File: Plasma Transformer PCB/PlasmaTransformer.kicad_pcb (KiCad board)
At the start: 2 copper layers, 90 x 90 mm, 65 parts, among them J1 Barrel_Jack_MountingPin, J11 Screw_Terminal_01x01, J12 Screw_Terminal_01x01, J2 Conn_01x02_Pin, J3 Conn_Coaxial, J4 Conn_02x04_Odd_Even, J5 Conn_Coaxial, J6 Conn_02x04_Odd_Even, J8 AudioJack3, M1 Fan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

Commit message: convert tank caps to push fit sockets
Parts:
- added J10: Conn_01x01_Socket, ALibrary:H8501-05, F.Cu at (89.0, 121.5)
- added J13: Conn_01x01_Socket, ALibrary:H8501-05, F.Cu at (89.0, 111.5)
- added J14: Conn_01x01_Socket, ALibrary:H8501-05, F.Cu at (83.5, 121.5)
- added J15: Conn_01x01_Socket, ALibrary:H8501-05, F.Cu at (83.5, 111.5)
- added J16: Conn_01x01_Socket, ALibrary:H8501-05, F.Cu at (78.0, 121.5)
- added J17: Conn_01x01_Socket, ALibrary:H8501-05, F.Cu at (78.0, 111.5)
- added J18: Conn_01x01_Socket, ALibrary:H8501-05, F.Cu at (72.5, 121.5)
- added J19: Conn_01x01_Socket, ALibrary:H8501-05, F.Cu at (72.5, 111.5)
- added J20: Conn_01x01_Socket, ALibrary:H8501-05, F.Cu at (67.0, 121.5)
- added J21: Conn_01x01_Socket, ALibrary:H8501-05, F.Cu at (67.0, 111.5)
- added J7: Conn_01x01_Socket, ALibrary:H8501-05, F.Cu at (94.5, 121.5)
- added J9: Conn_01x01_Socket, ALibrary:H8501-05, F.Cu at (94.5, 111.5)

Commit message: WIP rev 5 rebase
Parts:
- removed J10, J13, J14, J15, J16, J17, J18, J19, J20, J21, J7, J9: Conn_01x01_Socket, ALibrary:H8501-05
- added C25: 4.7uF, Capacitor_SMD:C_1210_3225Metric, F.Cu at (155.3, 96.6)
- added C26: 4.7uF, Capacitor_SMD:C_1210_3225Metric, F.Cu at (155.3, 100.8)
- added C27: 100nF, Capacitor_SMD:C_0805_2012Metric, F.Cu at (169.1, 82.4)
- added C28: 100nF, Capacitor_SMD:C_0805_2012Metric, F.Cu at (169.1, 85.4)
- added C29: 22uF, Capacitor_SMD:C_0805_2012Metric, F.Cu at (169.1, 88.4)
- added L3: 56uH, Inductor_SMD:L_Bourns_SRR1210A, F.Cu at (159.7, 87.7)
- added R1: 100k, Resistor_SMD:R_0805_2012Metric, F.Cu at (160.3, 95.9)
- added R10: 7.15k, Resistor_SMD:R_0805_2012Metric, F.Cu at (160.3, 98.9)
- added U1: LMR51610YDBVR, Package_TO_SOT_SMD:SOT-23-6, F.Cu at (165.1, 96.8)
- D5, D6, D7, D8: footprint Diode_SMD:D_SMB -> Diode_SMD:D_SMF
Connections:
- net Net-(D1-K) renamed /REF10V
- net Net-(SW1-A) renamed /VIN
- C1 pad 1: Net-(J10-Pin_1) -> Net-(J12-Pin_1)
- C12 pad 2: Net-(J2-Pin_1) -> +V
- C13 pad 2: Net-(J2-Pin_1) -> +V
- C14 pad 1: Net-(J10-Pin_1) -> /DRAIN
- C16 pad 1: Net-(J10-Pin_1) -> Net-(J12-Pin_1)
- C17 pad 1: Net-(J10-Pin_1) -> Net-(J12-Pin_1)
- C18 pad 1: Net-(J10-Pin_1) -> Net-(J12-Pin_1)
- C19 pad 1: Net-(J10-Pin_1) -> Net-(J12-Pin_1)
- C2 pad 1: Net-(J2-Pin_1) -> +V
- C20 pad 1: Net-(J10-Pin_1) -> Net-(J12-Pin_1)
- J12 pad 1: Net-(J10-Pin_1) -> Net-(J12-Pin_1)
- J2 pad 1: Net-(J2-Pin_1) -> +12V
- L2 pad 1: Net-(J2-Pin_1) -> +V
- R2 pad 1: Net-(J2-Pin_1) -> +12V
- SW1 pad 2: Net-(J2-Pin_1) -> +V
- TP2 pad 1: Net-(J2-Pin_1) -> +V
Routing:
- net Net-(J2-Pin_1): track 128.0 -> 0.00 mm
- net (no net): track 0.00 -> 128.0 mm
- net Net-(J12-Pin_1): track 0.00 -> 78.5 mm
- net Net-(J10-Pin_1): track 78.5 -> 0.00 mm
- net Net-(D6-A): track 70.2 -> 71.8 mm
- net Net-(D5-K): track 51.4 -> 50.7 mm
- added copper zone on F.Cu, net +V
- removed copper zone on F.Cu, net Net-(J2-Pin_1)
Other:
- board text added: "REV 5 SEPT 2025 E. CHIU"
- board text removed: "REV 4 JULY 2025 E. CHIU"

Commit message: WIP layout
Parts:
- L3: value 56uH -> 22uH; footprint Inductor_SMD:L_Bourns_SRR1210A -> Inductor_SMD:L_Coilcraft_2222SQ-90N
- moved C28 35.6 mm to (133.6, 88.0), turned to 90 degrees
- moved C27 34.3 mm to (134.8, 81.4), turned to 180 degrees
- moved U1 32.4 mm to (135.2, 84.2), turned to 180 degrees
- moved C26 29.9 mm to (135.3, 78.5)
- moved C25 29.4 mm to (135.3, 75.0)
- moved C29 25.4 mm to (143.7, 88.1), turned to 90 degrees
- moved R10 25.0 mm to (139.4, 85.1), turned to 180 degrees
- moved L3 20.9 mm to (138.9, 89.8)
- moved R1 20.4 mm to (143.0, 85.1), turned to 180 degrees
- moved TP2 2.32 mm to (140.2, 95.3)
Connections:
- net Net-(U1-SW) renamed /12VSW
- C14 pad 1: /DRAIN -> Net-(J12-Pin_1)
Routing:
- net (no net): track 128.0 -> 0.00 mm
- net +V: track 0.00 -> 123.5 mm, vias 0 -> 1
- net +12V: track 0.00 -> 103.8 mm, vias 0 -> 2
- net GND: track 354.3 -> 369.4 mm, vias 8 -> 11
- net Net-(U1-FB): track 0.00 -> 8.34 mm
- net Net-(U1-CB): track 0.00 -> 3.12 mm
- added copper zone on F.Cu, net /12VSW
- added copper zone on B.Cu, net GND
- added copper zone on F.Cu, net GND

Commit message: WIP layout
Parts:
- moved J3 1.50 mm to (61.0, 92.0)
- moved J5 1.50 mm to (61.0, 78.0)
- moved R8 1.00 mm to (69.0, 78.1)
- moved R7 1.00 mm to (67.2, 85.2)
- moved C25 0.40 mm to (135.7, 75.0)
- moved C26 0.40 mm to (135.7, 78.5)
- moved C27 0.40 mm to (135.2, 81.4)
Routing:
- net /DRAIN: track 175.2 -> 173.4 mm
- net Net-(J3-In): track 10.6 -> 11.9 mm
- net +V: track 123.5 -> 122.3 mm
- net /GATE: track 82.2 -> 81.1 mm
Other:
- board text added: "12- 60V IN"
- board text removed: "15- 24V IN"

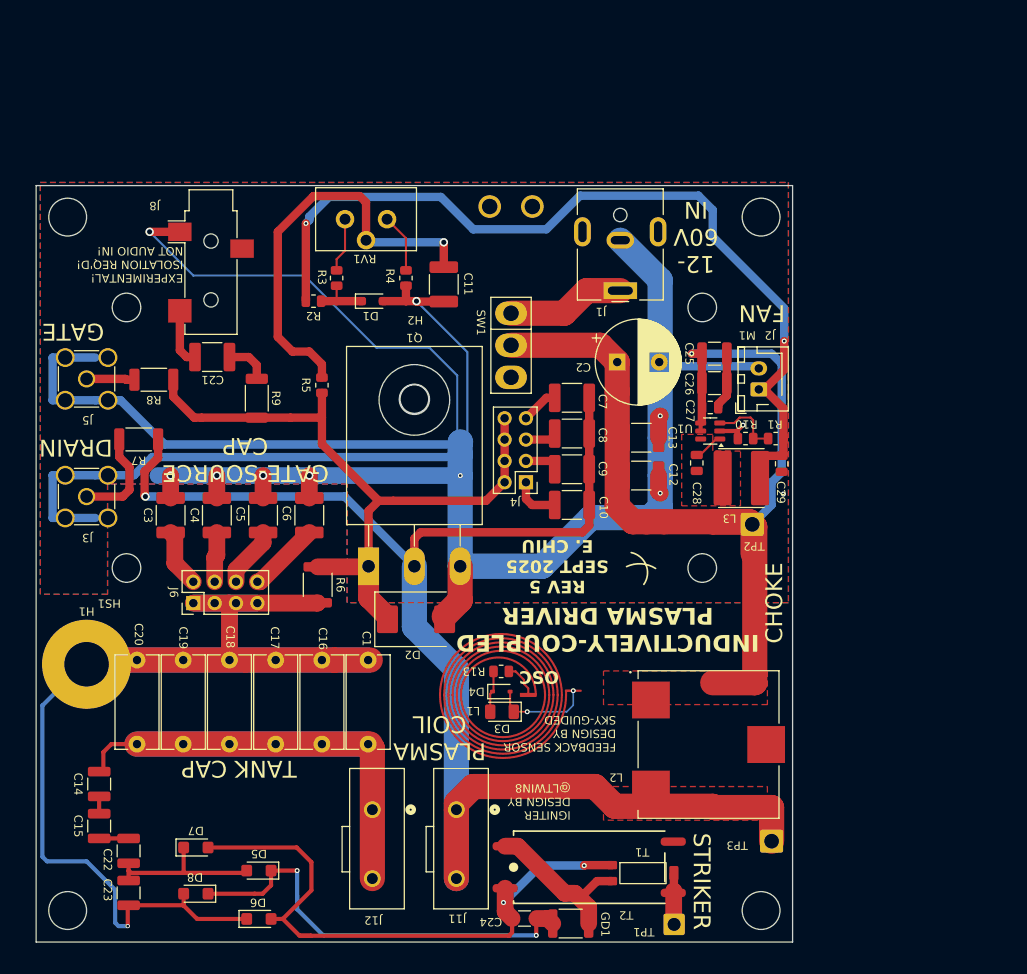
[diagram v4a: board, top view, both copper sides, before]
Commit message: improvements to ease of assembly, increased use of solid pours, layout complete, 1st DRC check complete.
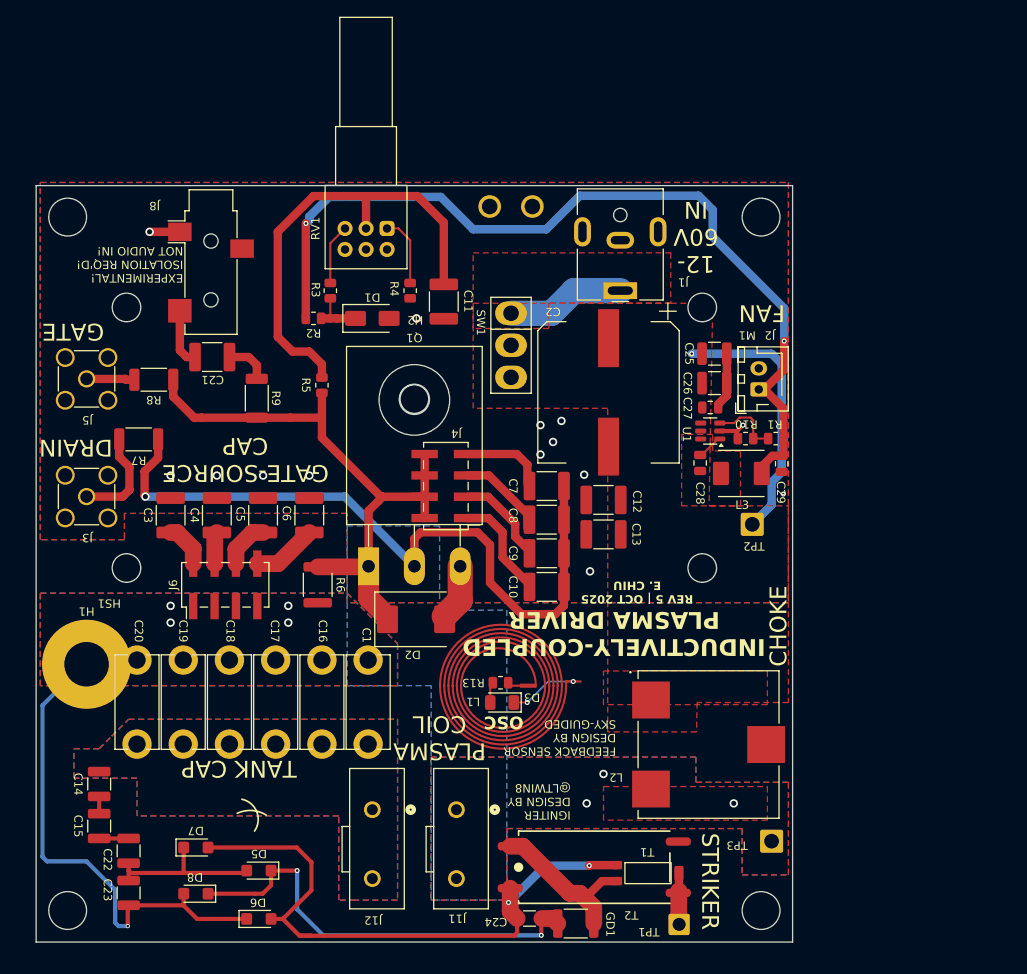
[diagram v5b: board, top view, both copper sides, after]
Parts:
- removed D4: D, Diode_SMD:D_SOD-323
- added J10: Conn_01x01_Socket, ALibrary:H8501-05, F.Cu at (89.0, 121.5)
- added J13: Conn_01x01_Socket, ALibrary:H8501-05, F.Cu at (89.0, 111.5)
- added J14: Conn_01x01_Socket, ALibrary:H8501-05, F.Cu at (83.5, 121.5)
- added J15: Conn_01x01_Socket, ALibrary:H8501-05, F.Cu at (83.5, 111.5)
- added J16: Conn_01x01_Socket, ALibrary:H8501-05, F.Cu at (78.0, 121.5)
- added J17: Conn_01x01_Socket, ALibrary:H8501-05, F.Cu at (78.0, 111.5)
- added J18: Conn_01x01_Socket, ALibrary:H8501-05, F.Cu at (72.5, 121.5)
- added J19: Conn_01x01_Socket, ALibrary:H8501-05, F.Cu at (72.5, 111.5)
- added J20: Conn_01x01_Socket, ALibrary:H8501-05, F.Cu at (67.0, 121.5)
- added J21: Conn_01x01_Socket, ALibrary:H8501-05, F.Cu at (67.0, 111.5)
- added J7: Conn_01x01_Socket, ALibrary:H8501-05, F.Cu at (94.5, 121.5)
- added J9: Conn_01x01_Socket, ALibrary:H8501-05, F.Cu at (94.5, 111.5)
- C2: footprint Capacitor_THT:CP_Radial_D10.0mm_P5.00mm -> ALibrary:CP_Elec_16x17.5_FK_Series
- D1: footprint Diode_SMD:D_SOD-323_HandSoldering -> Diode_SMD:D_SMA
- J4, J6: footprint Connector_PinHeader_2.54mm:PinHeader_2x04_P2.54mm_Vertical -> Connector_PinHeader_2.54mm:PinHeader_2x04_P2.54mm_Vertical_SMD
- L3: footprint Inductor_SMD:L_Coilcraft_2222SQ-90N -> ALibrary:L_Pana_PCC-KVP_5.5x5mm
- RV1: footprint ALibrary:SMC10H04-102A2020MTA -> ALibrary:Bourns-Potentiometer-PTD902-2
- moved C13 12.3 mm to (122.5, 96.5), turned to 0 degrees
- moved C7 10.9 mm to (115.8, 90.8)
- moved C8 10.7 mm to (115.8, 94.8)
- moved C9 10.4 mm to (115.8, 98.8)
- moved C10 10.2 mm to (115.8, 102.8)
- moved J4 9.54 mm to (103.8, 90.8)
- moved C12 5.35 mm to (122.5, 92.4), turned to 0 degrees
- moved J6 4.38 mm to (77.5, 102.5)
- moved C2 3.75 mm to (123.1, 79.6), turned to -90 degrees
- moved RV1 2.73 mm to (96.8, 60.1), turned to -90 degrees
- moved C11 2.05 mm to (103.5, 68.8)
- moved D1 2.05 mm to (95.0, 70.8)
- moved R2 2.05 mm to (88.0, 70.8)
- moved R3 1.68 mm to (90.0, 67.5)
- moved R4 1.58 mm to (99.5, 67.5)
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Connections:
- net Net-(D6-K) renamed /FEEDBACK
- net Net-(J12-Pin_1) renamed /RF-NODE
- RV1 pad 1: Net-(R3-Pad2) -> Net-(R4-Pad1)
- RV1 pad 3: Net-(R4-Pad1) -> Net-(R3-Pad2)
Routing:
- net GND: track 369.4 -> 20.3 mm, vias 11 -> 14
- net /FEEDBACK: track 164.3 -> 61.9 mm, vias 1 -> 5
- net +V: track 122.3 -> 31.8 mm
- net /DRAIN: track 173.4 -> 83.2 mm, vias 1 -> 4
- net /RF-NODE: track 78.5 -> 0.32 mm
- net /GATE: track 81.1 -> 70.7 mm
- net Net-(J4-Pin_5): track 2.70 -> 11.3 mm
- net Net-(J4-Pin_3): track 4.47 -> 11.3 mm
- net Net-(J4-Pin_1): track 5.70 -> 12.1 mm
- net Net-(J4-Pin_7): track 4.43 -> 9.95 mm
- net Net-(C11-Pad2): track 50.1 -> 54.7 mm, vias 1 -> 0
- net Net-(D3-K): track 11.7 -> 8.73 mm
- net Net-(D3-A): track 4.96 -> 2.14 mm
- net Net-(J6-Pin_4): track 5.97 -> 3.81 mm
- net Net-(J6-Pin_2): track 6.98 -> 5.27 mm
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- added copper zone on B.Cu, net /DRAIN
- added copper zone on B.Cu, net /FEEDBACK
- added copper zone on F.Cu, net /FEEDBACK
- added copper zone on B.Cu, net /RF-NODE
- added copper zone on F.Cu, net /RF-NODE
- added copper zone on F.Cu, net /VIN
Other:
- board text added: "REV 5 | OCT 2025 E. CHIU"
- board text removed: "REV 5 SEPT 2025 E. CHIU"

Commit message: clean up for manufacturing
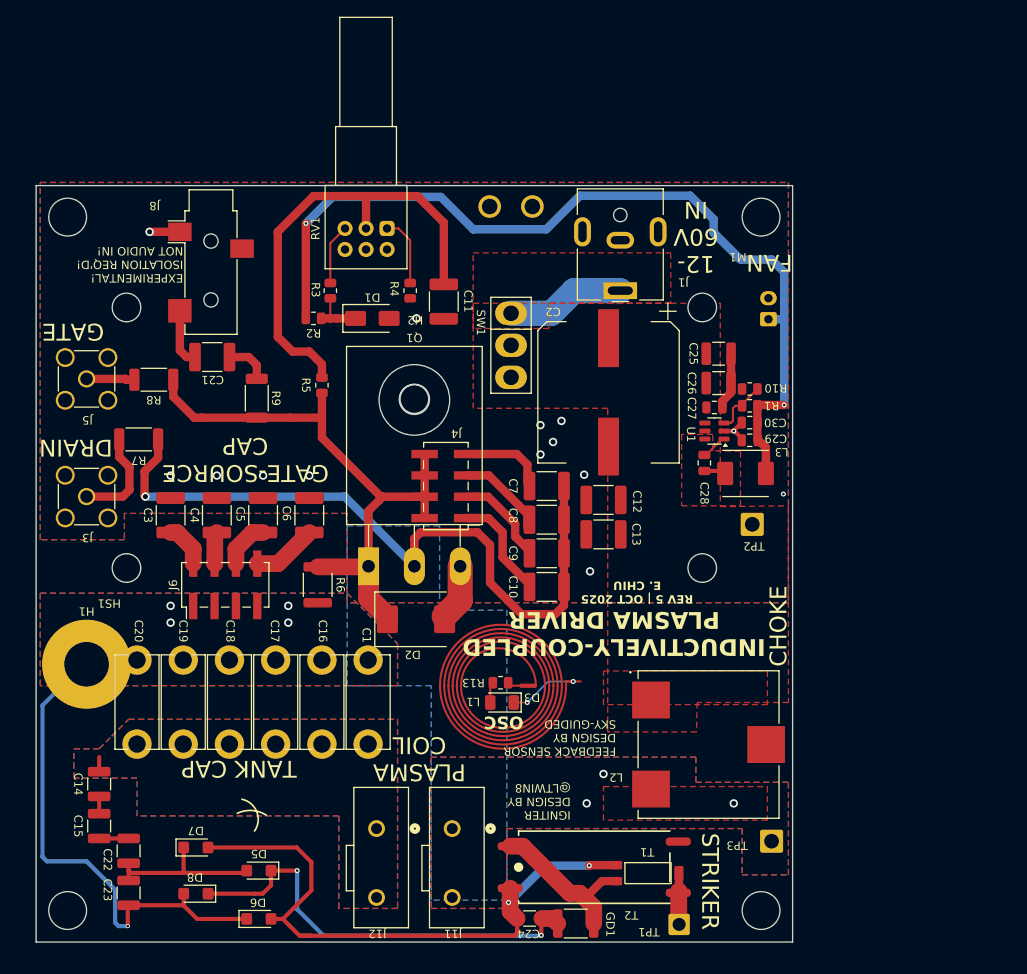
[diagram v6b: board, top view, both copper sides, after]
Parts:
- added C30: 10uF, Capacitor_SMD:C_0805_2012Metric, F.Cu at (139.9, 83.2)
- J2: footprint Connector_JST:JST_XH_B2B-XH-AM_1x02_P2.50mm_Vertical -> Connector_JST:JST_XH_B2B-XH-A_1x02_P2.50mm_Vertical; moved to B.Cu
- moved J2 8.43 mm to (142.1, 70.9)
- moved R10 5.92 mm to (139.9, 79.2)
- moved R1 4.98 mm to (139.9, 81.2)
- moved C29 4.72 mm to (139.9, 85.3), turned to 0 degrees
- moved J11 2.30 mm to (104.5, 131.5)
- moved J12 2.30 mm to (95.5, 131.5)
- moved C25 0.50 mm to (136.2, 75.0)
- moved C26 0.50 mm to (136.2, 78.5)
- moved C27 0.50 mm to (135.7, 81.4)
- moved C28 0.50 mm to (134.5, 88.0)
- moved L3 0.50 mm to (139.4, 89.2)
- moved U1 0.50 mm to (135.7, 84.2)
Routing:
- net +V: track 31.8 -> 0.04 mm, vias 1 -> 0
- net /12VSW: track 0.00 -> 2.60 mm
- net +12V: track 104.4 -> 106.7 mm
- net /RF-NODE: track 0.32 -> 2.04 mm
- net Net-(U1-FB): track 8.34 -> 6.63 mm
- net GND: track 20.3 -> 21.2 mm

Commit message: Clean up, silkscreens, BOM cleanup, title blocks, fab notes, generate manufacturing files
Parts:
- D1: value 10V -> 10V Zener
- D2: value 5.0SMDJ15CA -> 15V TVS
- GD1: value 300V -> 300V GDT
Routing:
- net /DRAIN: vias 4 -> 5
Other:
- board text added: "FAB NOTES: 1. FINISH: HASL LEAD FREE, ALTERNATE ENIG OK 2. SOLDERMASK: WHITE 3. SILKSCREEN: BLACK 4. LAYERS: 2 5. TOP AND BOTTOM WEIGHT: 1OZ 6. INNER LAYERS WEIGHT: 1OZ 7. TRACE/SPACE: 6MIL/6MIL 8. MINIMUM DRILL: 0.3MM 9. FINISHED THICKNESS: 1.6MM 10: CONTROLLED IMPEDANCE: NO 11. ITAR: NO 12. BOARD DIMENSIONS: 90MM x 90MM ASSY NOTES: 1. CLASS 2 ASSEMBLY 2. LEAD-FREE SOLDER 3. DO NOT POPULATE REFE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"
- board text added: "SN"
